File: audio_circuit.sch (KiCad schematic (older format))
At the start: 20 parts, among them T1 SM-LP-5001, T2 SM-LP-5001

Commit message: Fixed wrong footprint C1 [#21]
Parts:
- C1: footprint liteon:LTV-816S -> Capacitor_SMD:C_0805_2012Metric_Pad1.15x1.40mm_HandSolder
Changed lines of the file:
@@
 F 0 "C1" V 1698 1900 50  0000 C CNN
 F 1 "1uF" V 1789 1900 50  0000 C CNN
-F 2 "liteon:LTV-816S" H 1988 1750 50  0001 C CNN
+F 2 "Capacitor_SMD:C_0805_2012Metric_Pad1.15x1.40mm_HandSolder" H 1988 1750 50  0001 C CNN
 F 3 "~" H 1950 1900 50  0001 C CNN
 F 4 "80-C0805C105K3RAUTO" H 50  -4100 50  0001 C CNN "Mouser Best.Nr."

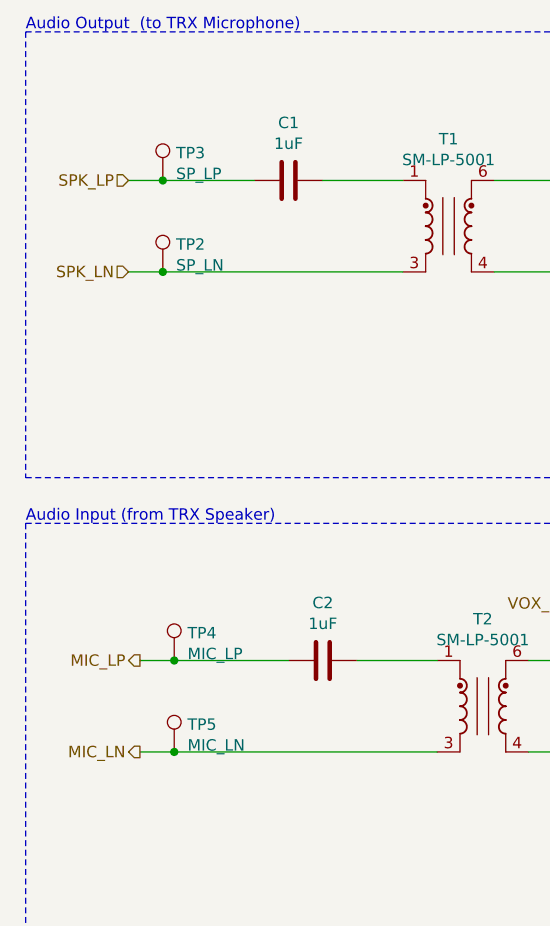
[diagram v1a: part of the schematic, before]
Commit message: Continued V5.0 Schematic Rework [#21]
- Replaced PTT_SEL Jumper from solder to pinheader
- Added blockin capacitors to WT32i
- Removed J9/10 solder jumpers
- Added separate PTT GND
- Changed hardware version indicator to 3.3V
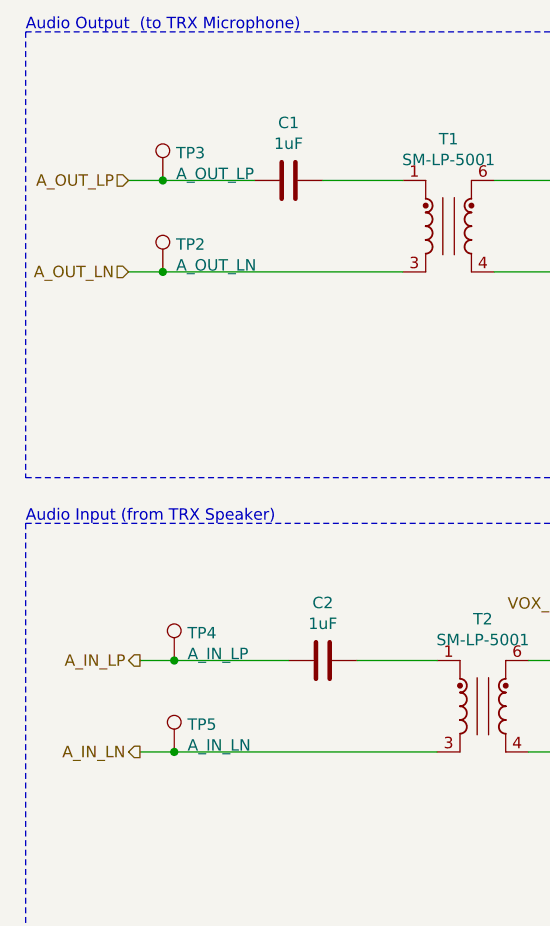
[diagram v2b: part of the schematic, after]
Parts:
- TP2: value SP_LN -> A_OUT_LN
- TP3: value SP_LP -> A_OUT_LP
- TP4: value MIC_LP -> A_IN_LP
- TP5: value MIC_LN -> A_IN_LN
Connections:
- net MIC_LN renamed A_IN_LN
- net MIC_LP renamed A_IN_LP
- net SPK_LN renamed A_OUT_LN
- net SPK_LP renamed A_OUT_LP
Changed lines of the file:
@@
 $EndDescr
 Text HLabel 1250 2300 0    50   Input ~ 0
-SPK_LN
+A_OUT_LN
 Text HLabel 5450 1900 2    50   Output ~ 0
 AUDIO_OUT
@@
 P 1450 4400
 F 0 "TP5" H 1508 4520 50  0000 L CNN
-F 1 "MIC_LN" H 1508 4429 50  0000 L CNN
+F 1 "A_IN_LN" H 1508 4429 50  0000 L CNN
 F 2 "TestPoint:TestPoint_Pad_D1.5mm" H 1650 4400 50  0001 C CNN
 F 3 "~" H 1650 4400 50  0001 C CNN
@@
 P 1400 2300
 F 0 "TP2" H 1458 2420 50  0000 L CNN
-F 1 "SP_LN" H 1458 2329 50  0000 L CNN
+F 1 "A_OUT_LN" H 1458 2329 50  0000 L CNN
 F 2 "TestPoint:TestPoint_Pad_D1.5mm" H 1600 2300 50  0001 C CNN
 F 3 "~" H 1600 2300 50  0001 C CNN
@@
 $EndComp
 Text HLabel 1250 1900 0    50   Input ~ 0
-SPK_LP
+A_OUT_LP
 $Comp
 L Connector:TestPoint TP3
@@
 P 1400 1900
 F 0 "TP3" H 1458 2020 50  0000 L CNN
-F 1 "SP_LP" H 1458 1929 50  0000 L CNN
+F 1 "A_OUT_LP" H 1458 1929 50  0000 L CNN
 F 2 "TestPoint:TestPoint_Pad_D1.5mm" H 1600 1900 50  0001 C CNN
 F 3 "~" H 1600 1900 50  0001 C CNN
@@
 P 1450 4000
 F 0 "TP4" H 1508 4120 50  0000 L CNN
-F 1 "MIC_LP" H 1508 4029 50  0000 L CNN
+F 1 "A_IN_LP" H 1508 4029 50  0000 L CNN
 F 2 "TestPoint:TestPoint_Pad_D1.5mm" H 1650 4000 50  0001 C CNN
 F 3 "~" H 1650 4000 50  0001 C CNN
@@
 $EndComp
 Text HLabel 1300 4400 0    50   Output ~ 0
-MIC_LN
+A_IN_LN
 Text HLabel 1300 4000 0    50   Output ~ 0
-MIC_LP
+A_IN_LP
 $Comp
 L Connector:TestPoint TP8

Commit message: Reworked PCB [#19][#21][#22][#23]
* Reworked PCB with new v5.0 schematic
* Fixed position of mounting holes
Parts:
- TP1: footprint TestPoint:TestPoint_Pad_4.0x4.0mm -> TestPoint:TestPoint_Pad_D1.5mm
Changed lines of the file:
@@
 Text HLabel 1300 4000 0    50   Output ~ 0
 A_IN_LP
-$Comp
-L Connector:TestPoint TP8
-U 1 1 5C0DF1AC
-P 4750 4400
-F 0 "TP8" H 4808 4520 50  0000 L CNN
-F 1 "TRX_GND" H 4808 4429 50  0000 L CNN
-F 2 "TestPoint:TestPoint_Pad_4.0x4.0mm" H 4950 4400 50  0001 C CNN
-F 3 "~" H 4950 4400 50  0001 C CNN
-F 4 "-" H 200 -2450 50  0001 C CNN "Mouser Best.Nr."
-	1    4750 4400
-	1    0    0    -1
-$EndComp
 Wire Wire Line
 	4750 3750 5300 3750
@@
 	1    0    0    -1
 $EndComp
-Wire Wire Line
-	4750 4550 4750 4400
 Wire Wire Line
 	3550 1900 3900 1900
@@
 F 0 "TP1" H 5008 2420 50  0000 L CNN
 F 1 "MIC_GND" H 5008 2329 50  0000 L CNN
-F 2 "TestPoint:TestPoint_Pad_4.0x4.0mm" H 5150 2300 50  0001 C CNN
+F 2 "TestPoint:TestPoint_Pad_D1.5mm" H 5150 2300 50  0001 C CNN
 F 3 "~" H 5150 2300 50  0001 C CNN
 F 4 "-" H 400 -4550 50  0001 C CNN "Mouser Best.Nr."
@@
 F 3 "" H 4050 4550 50  0001 C CNN
 	1    4050 4550
-	1    0    0    -1
-$EndComp
-$Comp
-L power:GND #PWR019
-U 1 1 5E42553D
-P 4750 4550
-F 0 "#PWR019" H 4750 4300 50  0001 C CNN
-F 1 "GND" H 4755 4377 50  0000 C CNN
-F 2 "" H 4750 4550 50  0001 C CNN
-F 3 "" H 4750 4550 50  0001 C CNN
-	1    4750 4550
 	1    0    0    -1
 $EndComp
@@
 Wire Wire Line
 	3000 4000 3400 4000
+$Comp
+L power:GND #PWR019
+U 1 1 5E42553D
+P 4750 4550
+F 0 "#PWR019" H 4750 4300 50  0001 C CNN
+F 1 "GND" H 4755 4377 50  0000 C CNN
+F 2 "" H 4750 4550 50  0001 C CNN
+F 3 "" H 4750 4550 50  0001 C CNN
+	1    4750 4550
+	1    0    0    -1
+$EndComp
+Wire Wire Line
+	4750 4550 4750 4400
+$Comp
+L Connector:TestPoint TP8
+U 1 1 5C0DF1AC
+P 4750 4400
+F 0 "TP8" H 4808 4520 50  0000 L CNN
+F 1 "TRX_GND" H 4808 4429 50  0000 L CNN
+F 2 "TestPoint:TestPoint_Pad_4.0x4.0mm" H 4950 4400 50  0001 C CNN
+F 3 "~" H 4950 4400 50  0001 C CNN
+F 4 "-" H 200 -2450 50  0001 C CNN "Mouser Best.Nr."
+	1    4750 4400
+	1    0    0    -1
+$EndComp
 $EndSCHEMATC

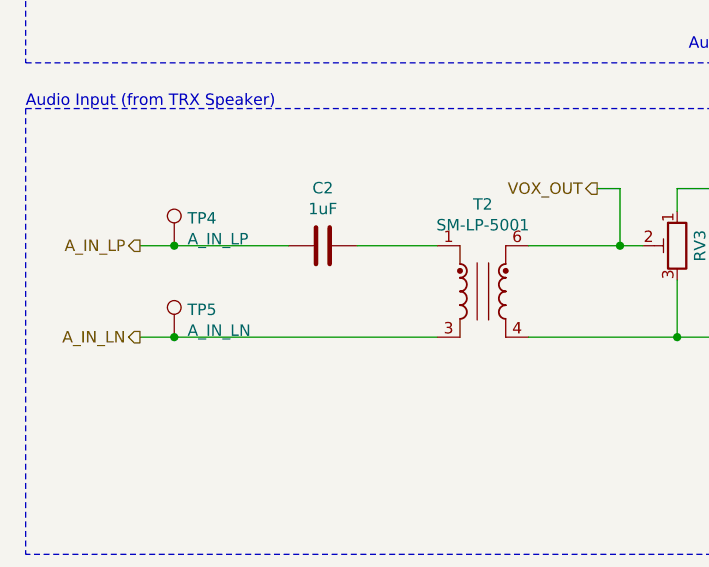
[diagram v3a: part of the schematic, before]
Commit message: Flipped T2 for better grounding [#25]
* Flipped input ports of T2 as there as no direct TRX-GND path from RV3 to T2
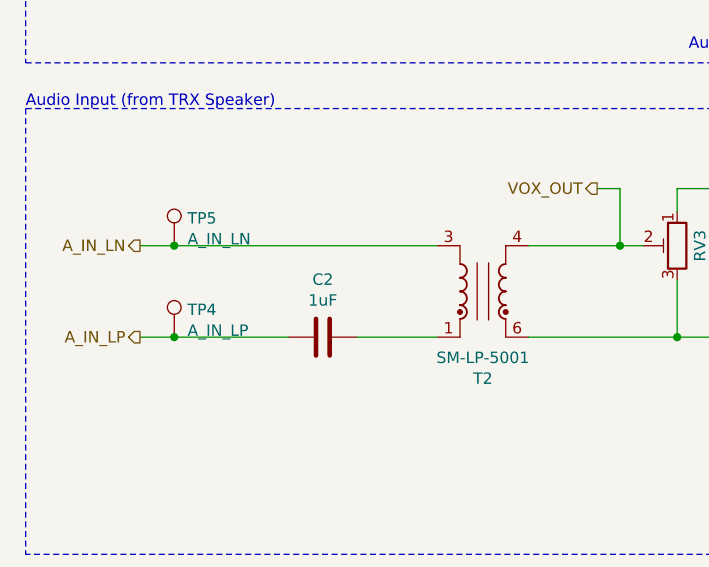
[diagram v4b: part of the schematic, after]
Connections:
- net GND: now also T2.6; no longer T2.4
- net VOX_OUT: now also T2.4; no longer T2.6
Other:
- moved on the sheet: C2, TP4, TP5
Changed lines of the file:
@@
 L Device:C C2
 U 1 1 5BFC0997
-P 2100 4000
-F 0 "C2" V 1848 4000 50  0000 C CNN
-F 1 "1uF" V 1939 4000 50  0000 C CNN
-F 2 "Capacitor_SMD:C_0805_2012Metric_Pad1.15x1.40mm_HandSolder" H 2138 3850 50  0001 C CNN
-F 3 "~" H 2100 4000 50  0001 C CNN
-F 4 "80-C0805C105K3RAUTO" H 200 -2000 50  0001 C CNN "Mouser Best.Nr."
-	1    2100 4000
+P 2100 4400
+F 0 "C2" V 1848 4400 50  0000 C CNN
+F 1 "1uF" V 1939 4400 50  0000 C CNN
+F 2 "Capacitor_SMD:C_0805_2012Metric_Pad1.15x1.40mm_HandSolder" H 2138 4250 50  0001 C CNN
+F 3 "~" H 2100 4400 50  0001 C CNN
+F 4 "80-C0805C105K3RAUTO" H 200 -1600 50  0001 C CNN "Mouser Best.Nr."
+	1    2100 4400
 	0    1    1    0
 $EndComp
@@
 $EndComp
 Wire Wire Line
+	1300 4400 1450 4400
+Wire Wire Line
 	1300 4000 1450 4000
-Wire Wire Line
-	1300 4400 1450 4400
-Connection ~ 1450 4000
-Wire Wire Line
-	1450 4000 1950 4000
+Connection ~ 1450 4400
+Wire Wire Line
+	1450 4400 1950 4400
 $Comp
 L Connector:TestPoint TP5
 U 1 1 5C77A456
-P 1450 4400
-F 0 "TP5" H 1508 4520 50  0000 L CNN
-F 1 "A_IN_LN" H 1508 4429 50  0000 L CNN
-F 2 "TestPoint:TestPoint_Pad_D1.5mm" H 1650 4400 50  0001 C CNN
-F 3 "~" H 1650 4400 50  0001 C CNN
-F 4 "-" H 50  -1950 50  0001 C CNN "Mouser Best.Nr."
-	1    1450 4400
-	1    0    0    -1
-$EndComp
-Connection ~ 1450 4400
+P 1450 4000
+F 0 "TP5" H 1508 4120 50  0000 L CNN
+F 1 "A_IN_LN" H 1508 4029 50  0000 L CNN
+F 2 "TestPoint:TestPoint_Pad_D1.5mm" H 1650 4000 50  0001 C CNN
+F 3 "~" H 1650 4000 50  0001 C CNN
+F 4 "-" H 50  -2350 50  0001 C CNN "Mouser Best.Nr."
+	1    1450 4000
+	1    0    0    -1
+$EndComp
 Text Notes 800  1250 0    50   ~ 0
 Audio Output  (to TRX Microphone)
@@
 L Connector:TestPoint TP4
 U 1 1 5C77A38C
-P 1450 4000
-F 0 "TP4" H 1508 4120 50  0000 L CNN
-F 1 "A_IN_LP" H 1508 4029 50  0000 L CNN
-F 2 "TestPoint:TestPoint_Pad_D1.5mm" H 1650 4000 50  0001 C CNN
-F 3 "~" H 1650 4000 50  0001 C CNN
-F 4 "-" H 50  -1900 50  0001 C CNN "Mouser Best.Nr."
-	1    1450 4000
-	1    0    0    -1
-$EndComp
+P 1450 4400
+F 0 "TP4" H 1508 4520 50  0000 L CNN
+F 1 "A_IN_LP" H 1508 4429 50  0000 L CNN
+F 2 "TestPoint:TestPoint_Pad_D1.5mm" H 1650 4400 50  0001 C CNN
+F 3 "~" H 1650 4400 50  0001 C CNN
+F 4 "-" H 50  -1500 50  0001 C CNN "Mouser Best.Nr."
+	1    1450 4400
+	1    0    0    -1
+$EndComp
+Text HLabel 1300 4000 0    50   Output ~ 0
+A_IN_LN
 Text HLabel 1300 4400 0    50   Output ~ 0
-A_IN_LN
-Text HLabel 1300 4000 0    50   Output ~ 0
 A_IN_LP
 Wire Wire Line
@@
 F 3 "~" H 2800 4200 50  0001 C CNN
 	1    2800 4200
-	1    0    0    -1
+	1    0    0    1
 $EndComp
 Wire Wire Line
@@
 	2850 2300 3400 2300
 Wire Wire Line
-	2250 4000 2600 4000
-Wire Wire Line
-	1450 4400 2600 4400
-Wire Wire Line
 	3000 4400 3650 4400
 Wire Wire Line
@@
 	1    0    0    -1
 $EndComp
+Wire Wire Line
+	1450 4000 2600 4000
+Connection ~ 1450 4000
+Wire Wire Line
+	2250 4400 2600 4400
 $EndSCHEMATC

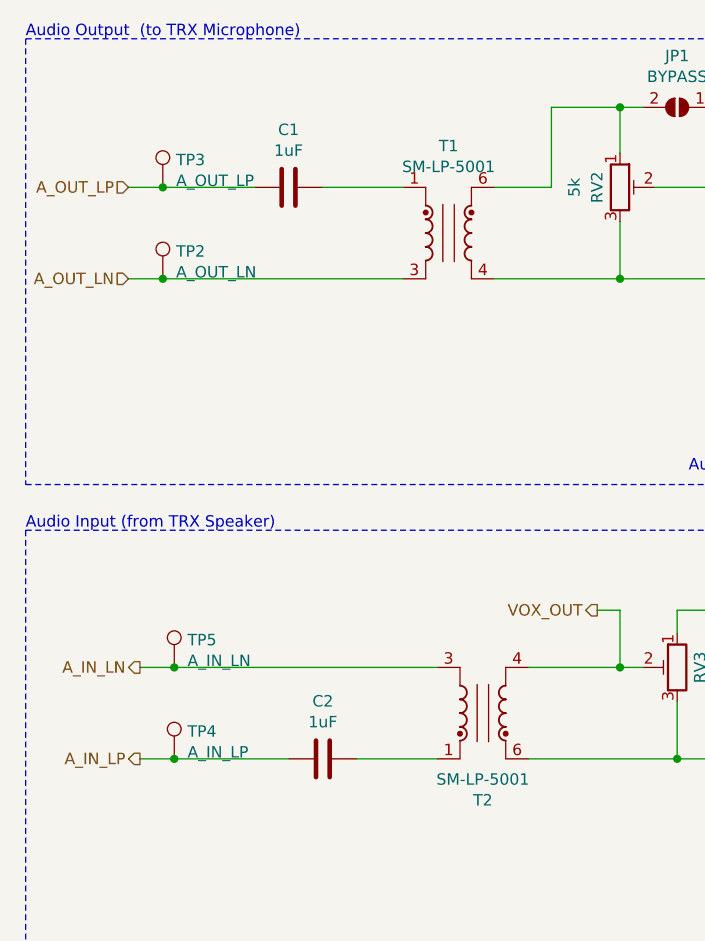
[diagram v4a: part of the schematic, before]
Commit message: PCB enhancements [#25]
* Removed C1 and C2
* Modified symmetric audio path
* Modified VOX path
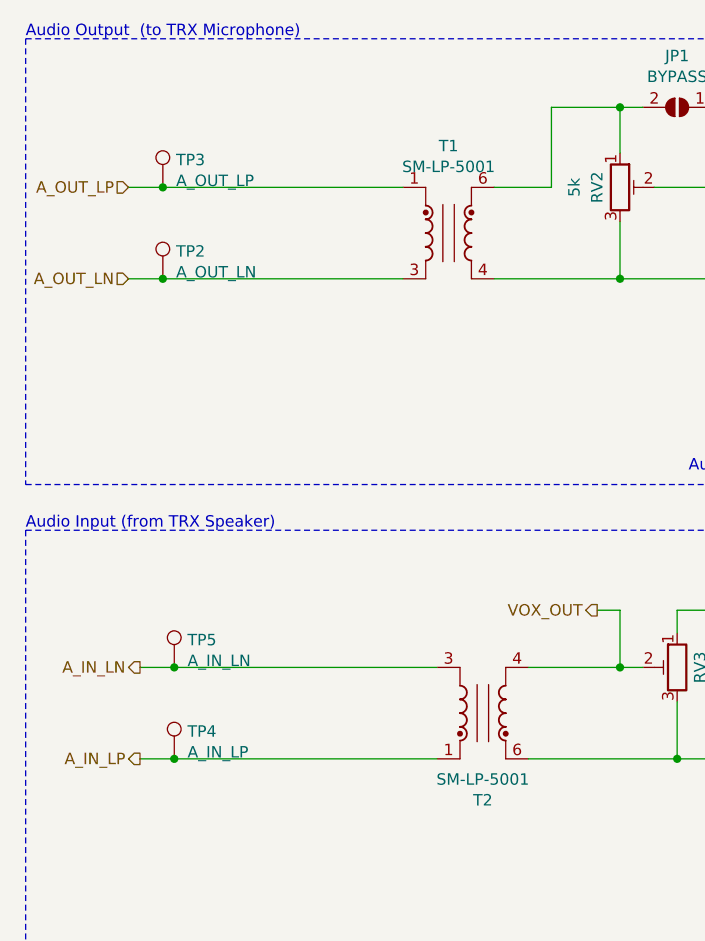
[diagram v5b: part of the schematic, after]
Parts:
- removed C1, C2: 1uF, Capacitor_SMD:C_0805_2012Metric_Pad1.15x1.40mm_HandSolder, symbol Device:C
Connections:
- net A_IN_LP: now also T2.1
- net A_OUT_LP: now also T1.1
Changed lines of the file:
@@
 	1    0    0    -1
-$EndComp
-$Comp
-L Device:C C2
-U 1 1 5BFC0997
-P 2100 4400
-F 0 "C2" V 1848 4400 50  0000 C CNN
-F 1 "1uF" V 1939 4400 50  0000 C CNN
-F 2 "Capacitor_SMD:C_0805_2012Metric_Pad1.15x1.40mm_HandSolder" H 2138 4250 50  0001 C CNN
-F 3 "~" H 2100 4400 50  0001 C CNN
-F 4 "80-C0805C105K3RAUTO" H 200 -1600 50  0001 C CNN "Mouser Best.Nr."
-	1    2100 4400
-	0    1    1    0
-$EndComp
-$Comp
-L Device:C C1
-U 1 1 5C774C08
-P 1950 1900
-F 0 "C1" V 1698 1900 50  0000 C CNN
-F 1 "1uF" V 1789 1900 50  0000 C CNN
-F 2 "Capacitor_SMD:C_0805_2012Metric_Pad1.15x1.40mm_HandSolder" H 1988 1750 50  0001 C CNN
-F 3 "~" H 1950 1900 50  0001 C CNN
-F 4 "80-C0805C105K3RAUTO" H 50  -4100 50  0001 C CNN "Mouser Best.Nr."
-	1    1950 1900
-	0    1    1    0
 $EndComp
 Wire Wire Line
@@
 	1300 4000 1450 4000
 Connection ~ 1450 4400
-Wire Wire Line
-	1450 4400 1950 4400
 $Comp
 L Connector:TestPoint TP5
@@
 	1    0    0    -1
 $EndComp
-Wire Wire Line
-	1400 1900 1800 1900
 Connection ~ 1400 1900
 Connection ~ 1400 2300
@@
 $EndComp
 Wire Wire Line
-	2100 1900 2450 1900
-Wire Wire Line
 	1400 2300 2450 2300
 Wire Wire Line
@@
 Connection ~ 1450 4000
 Wire Wire Line
-	2250 4400 2600 4400
+	1400 1900 2450 1900
+Wire Wire Line
+	1450 4400 2600 4400
 $EndSCHEMATC

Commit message: BOM Update
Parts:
- T1, T2: Mouser Best.Nr. (none) -> 652-SM-LP-5001
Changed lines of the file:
@@
 F 2 "bourns:SM-LP-5001" H 2650 2100 50  0001 C CNN
 F 3 "~" H 2650 2100 50  0001 C CNN
+F 4 "652-SM-LP-5001" H 2650 2100 50  0001 C CNN "Mouser Best.Nr."
 	1    2650 2100
 	1    0    0    -1
@@
 F 2 "bourns:SM-LP-5001" H 2800 4200 50  0001 C CNN
 F 3 "~" H 2800 4200 50  0001 C CNN
+F 4 "652-SM-LP-5001" H 2800 4200 50  0001 C CNN "Mouser Best.Nr."
 	1    2800 4200
 	1    0    0    1

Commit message: removed RV2 from order list
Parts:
- RV2: DNA (none) -> DNA
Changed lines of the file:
@@
 F 3 "~" H 3400 1900 50  0001 C CNN
 F 4 " 72-TS53YL-5K" H 550 -4100 50  0001 C CNN "Mouser Best.Nr."
+F 5 "DNA" H 3400 1900 50  0001 C CNN "DNA"
 	1    3400 1900
 	1    0    0    -1

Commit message: Fixed mouser order IDs
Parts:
- RV2, RV3: Mouser Best.Nr. 72-TS53YL-5K -> 72-TS53YL-5K
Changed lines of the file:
@@
 F 2 "Potentiometer_SMD:Potentiometer_Vishay_TS53YL_Vertical" H 3400 1900 50  0001 C CNN
 F 3 "~" H 3400 1900 50  0001 C CNN
-F 4 " 72-TS53YL-5K" H 550 -4100 50  0001 C CNN "Mouser Best.Nr."
+F 4 "72-TS53YL-5K" H 550 -4100 50  0001 C CNN "Mouser Best.Nr."
 F 5 "DNA" H 3400 1900 50  0001 C CNN "DNA"
 	1    3400 1900
@@
 F 2 "Potentiometer_SMD:Potentiometer_Vishay_TS53YL_Vertical" H 3650 4000 50  0001 C CNN
 F 3 "~" H 3650 4000 50  0001 C CNN
-F 4 " 72-TS53YL-5K" H 800 -2000 50  0001 C CNN "Mouser Best.Nr."
+F 4 "72-TS53YL-5K" H 800 -2000 50  0001 C CNN "Mouser Best.Nr."
 	1    3650 4000
 	-1   0    0    -1
